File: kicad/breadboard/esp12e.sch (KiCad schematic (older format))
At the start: 9 parts, among them J1 Conn_01x08, J3 Conn_01x08, SW1 SWITCH, SW2 SWITCH, U3 ESP-12E

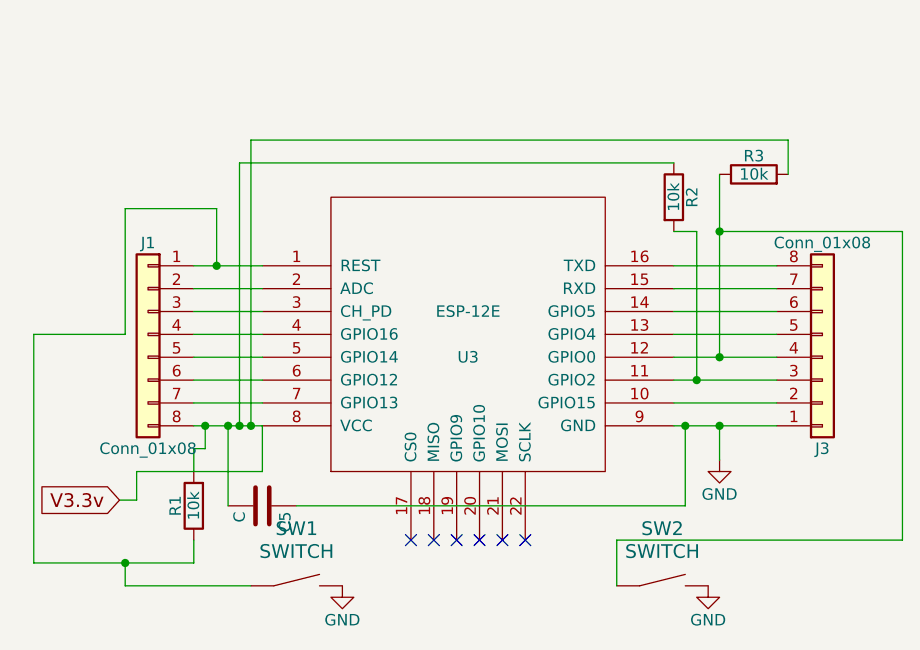
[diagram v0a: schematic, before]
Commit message: breadboard: fix the mistakes in esp12e board design
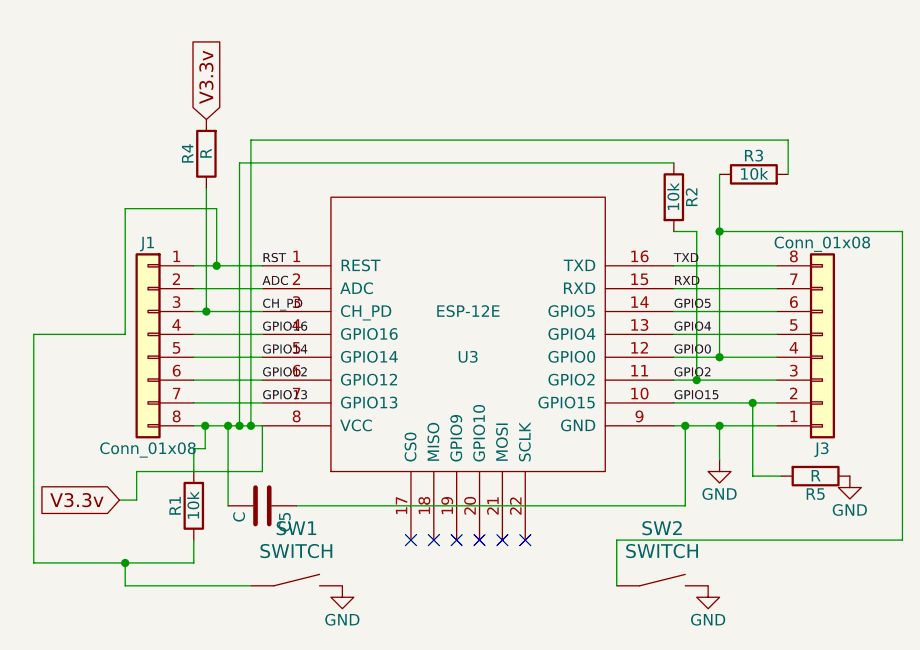
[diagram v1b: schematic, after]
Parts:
- added R4, R5: R, Resistors_SMD:R_0603_HandSoldering, symbol R
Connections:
- net GND: now also R5.1
- net V3.3v: now also R4.2
- net RST: now reaches J1.1 (Pin_1), R1.1, SW1.1, U3.1 (REST)
- net ADC: now reaches J1.2 (Pin_2), U3.2 (ADC)
- net CH_PD: now reaches J1.3 (Pin_3), U3.3 (CH_PD)
- net CH_PD: now also R4.1
- net GPIO16: now reaches J1.4 (Pin_4), U3.4 (GPIO16)
- net GPIO14: now reaches J1.5 (Pin_5), U3.5 (GPIO14)
- net GPIO12: now reaches J1.6 (Pin_6), U3.6 (GPIO12)
- net GPIO13: now reaches J1.7 (Pin_7), U3.7 (GPIO13)
- net GPIO15: now reaches J3.2 (Pin_2), U3.10 (GPIO15)
- net GPIO15: now also R5.2
- net GPIO2: now reaches J3.3 (Pin_3), R2.2, U3.11 (GPIO2)
- net GPIO0: now reaches J3.4 (Pin_4), R3.1, SW2.1, U3.12 (GPIO0)
- net GPIO4: now reaches J3.5 (Pin_5), U3.13 (GPIO4)
- net GPIO5: now reaches J3.6 (Pin_6), U3.14 (GPIO5)
- net RXD: now reaches J3.7 (Pin_7), U3.15 (RXD)
- net TXD: now reaches J3.8 (Pin_8), U3.16 (TXD)
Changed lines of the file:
@@
 	1    0    0    -1
 $EndComp
-Wire Wire Line
-	4600 3125 4900 3125
-Wire Wire Line
-	4600 3225 4900 3225
-Wire Wire Line
-	4600 3325 4900 3325
-Wire Wire Line
-	4600 3525 4900 3525
-Wire Wire Line
-	4600 3425 4900 3425
-Wire Wire Line
-	4600 3625 4900 3625
-Wire Wire Line
-	4600 3725 4900 3725
-Wire Wire Line
-	4600 3825 4900 3825
-Wire Wire Line
-	6700 3125 7150 3125
-Wire Wire Line
-	6700 3225 7150 3225
-Wire Wire Line
-	6700 3325 7150 3325
-Wire Wire Line
-	6700 3425 7150 3425
-Wire Wire Line
-	6700 3525 7150 3525
-Wire Wire Line
-	6700 3625 7150 3625
-Wire Wire Line
-	6700 3725 7150 3725
-Wire Wire Line
-	6700 3825 7150 3825
-Wire Wire Line
-	4750 4175 4750 3825
-Connection ~ 4750 3825
-Wire Wire Line
-	5050 4175 6750 4175
-Wire Wire Line
-	6750 4175 6750 3825
-Connection ~ 6750 3825
-Wire Wire Line
-	4600 4025 4600 3925
-Wire Wire Line
-	4600 3925 4650 3925
-Wire Wire Line
-	4650 3925 4650 3825
-Connection ~ 4650 3825
-Wire Wire Line
-	4600 4425 4600 4325
-Wire Wire Line
-	3900 4425 4600 4425
-Wire Wire Line
-	3900 4425 3900 3425
-Wire Wire Line
-	3900 3425 4300 3425
-Wire Wire Line
-	4300 3425 4300 2875
-Wire Wire Line
-	4300 2875 4700 2875
-Wire Wire Line
-	4700 2875 4700 3125
-Connection ~ 4700 3125
-Wire Wire Line
-	4300 4425 4300 4525
-Wire Wire Line
-	4300 4525 4850 4525
-Connection ~ 4300 4425
-Wire Wire Line
-	6900 2725 6900 3525
-Connection ~ 6900 3525
-Wire Wire Line
-	7200 2725 7200 2575
-Wire Wire Line
-	7200 2575 4850 2575
-Wire Wire Line
-	4850 2575 4850 3825
-Connection ~ 4850 3825
-Wire Wire Line
-	6700 2975 6800 2975
-Wire Wire Line
-	6800 2975 6800 3625
-Connection ~ 6800 3625
-Wire Wire Line
-	6700 2675 4800 2675
-Wire Wire Line
-	4800 2675 4800 3825
-Connection ~ 4800 3825
-Wire Wire Line
-	6450 4525 6450 4325
-Wire Wire Line
-	6450 4325 7700 4325
-Wire Wire Line
-	7700 4325 7700 2975
-Wire Wire Line
-	7700 2975 6900 2975
-Connection ~ 6900 2975
 $Comp
 L GND #PWR013
@@
 	1    0    0    -1
 $EndComp
-Connection ~ 6900 3825
-Wire Wire Line
-	6900 3975 6900 3825
 $Comp
 L GND #PWR015
@@
 Text GLabel 4275 4150 0    60   Input ~ 0
 V3.3v
+Text Label 6700 3125 0    39   ~ 0
+TXD
+Text Label 6700 3225 0    39   ~ 0
+RXD
+Text Label 6700 3325 0    39   ~ 0
+GPIO5
+Text Label 6700 3425 0    39   ~ 0
+GPIO4
+Text Label 6700 3525 0    39   ~ 0
+GPIO0
+Text Label 6700 3725 0    39   ~ 0
+GPIO15
+Text Label 6700 3625 0    39   ~ 0
+GPIO2
+Text Label 4900 3125 0    39   ~ 0
+RST
+Text Label 4900 3225 0    39   ~ 0
+ADC
+Text Label 4900 3325 0    39   ~ 0
+CH_PD
+Text Label 4900 3425 0    39   ~ 0
+GPIO16
+Text Label 4900 3525 0    39   ~ 0
+GPIO14
+Text Label 4900 3625 0    39   ~ 0
+GPIO12
+Text Label 4900 3725 0    39   ~ 0
+GPIO13
+$Comp
+L R R4
+U 1 1 5A0AD662
+P 4655 2635
+F 0 "R4" V 4735 2635 50  0000 C CNN
+F 1 "R" V 4655 2635 50  0000 C CNN
+F 2 "Resistors_SMD:R_0603_HandSoldering" V 4585 2635 50  0001 C CNN
+F 3 "" H 4655 2635 50  0001 C CNN
+	1    4655 2635
+	-1   0    0    1
+$EndComp
+Text GLabel 4655 2485 1    60   Input ~ 0
+V3.3v
+$Comp
+L R R5
+U 1 1 5A0AE1A4
+P 7320 4045
+F 0 "R5" V 7400 4045 50  0000 C CNN
+F 1 "R" V 7320 4045 50  0000 C CNN
+F 2 "Resistors_SMD:R_0603_HandSoldering" V 7250 4045 50  0001 C CNN
+F 3 "" H 7320 4045 50  0001 C CNN
+	1    7320 4045
+	0    1    1    0
+$EndComp
+Wire Wire Line
+	4600 3125 4900 3125
+Wire Wire Line
+	4600 3225 4900 3225
+Wire Wire Line
+	4600 3325 4900 3325
+Wire Wire Line
+	4600 3525 4900 3525
+Wire Wire Line
+	4600 3425 4900 3425
+Wire Wire Line
+	4600 3625 4900 3625
+Wire Wire Line
+	4600 3725 4900 3725
+Wire Wire Line
+	4600 3825 4900 3825
+Wire Wire Line
+	6700 3125 7150 3125
+Wire Wire Line
+	6700 3225 7150 3225
+Wire Wire Line
+	6700 3325 7150 3325
+Wire Wire Line
+	6700 3425 7150 3425
+Wire Wire Line
+	6700 3525 7150 3525
+Wire Wire Line
+	6700 3625 7150 3625
+Wire Wire Line
+	6700 3725 7150 3725
+Wire Wire Line
+	6700 3825 7150 3825
+Wire Wire Line
+	4750 4175 4750 3825
+Connection ~ 4750 3825
+Wire Wire Line
+	5050 4175 6750 4175
+Wire Wire Line
+	6750 4175 6750 3825
+Connection ~ 6750 3825
+Wire Wire Line
+	4600 4025 4600 3925
+Wire Wire Line
+	4600 3925 4650 3925
+Wire Wire Line
+	4650 3925 4650 3825
+Connection ~ 4650 3825
+Wire Wire Line
+	4600 4425 4600 4325
+Wire Wire Line
+	3900 4425 4600 4425
+Wire Wire Line
+	3900 4425 3900 3425
+Wire Wire Line
+	3900 3425 4300 3425
+Wire Wire Line
+	4300 3425 4300 2875
+Wire Wire Line
+	4300 2875 4700 2875
+Wire Wire Line
+	4700 2875 4700 3125
+Connection ~ 4700 3125
+Wire Wire Line
+	4300 4425 4300 4525
+Wire Wire Line
+	4300 4525 4850 4525
+Connection ~ 4300 4425
+Wire Wire Line
+	6900 2725 6900 3525
+Connection ~ 6900 3525
+Wire Wire Line
+	7200 2725 7200 2575
+Wire Wire Line
+	7200 2575 4850 2575
+Wire Wire Line
+	4850 2575 4850 3825
+Connection ~ 4850 3825
+Wire Wire Line
+	6700 2975 6800 2975
+Wire Wire Line
+	6800 2975 6800 3625
+Connection ~ 6800 3625
+Wire Wire Line
+	6700 2675 4800 2675
+Wire Wire Line
+	4800 2675 4800 3825
+Connection ~ 4800 3825
+Wire Wire Line
+	6450 4525 6450 4325
+Wire Wire Line
+	6450 4325 7700 4325
+Wire Wire Line
+	7700 4325 7700 2975
+Wire Wire Line
+	7700 2975 6900 2975
+Connection ~ 6900 2975
+Connection ~ 6900 3825
+Wire Wire Line
+	6900 3975 6900 3825
 Wire Wire Line
 	4275 4150 4350 4150
@@
 Wire Wire Line
 	4900 4025 4900 3825
+Wire Wire Line
+	4655 2785 4655 3325
+Connection ~ 4655 3325
+Wire Wire Line
+	7045 3725 7045 4045
+Wire Wire Line
+	7045 4045 7170 4045
+Connection ~ 7045 3725
+$Comp
+L GND #PWR016
+U 1 1 5A0AE489
+P 7470 4045
+F 0 "#PWR016" H 7470 3795 50  0001 C CNN
+F 1 "GND" H 7470 3895 50  0000 C CNN
+F 2 "" H 7470 4045 50  0001 C CNN
+F 3 "" H 7470 4045 50  0001 C CNN
+	1    7470 4045
+	1    0    0    -1
+$EndComp
 $EndSCHEMATC
